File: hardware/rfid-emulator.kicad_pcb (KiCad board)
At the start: 4 copper layers, 150 x 72 mm, 102 parts, among them J1 AVR-JTAG-10, J2 Micro_USB, J3 OSTTC020162, Q1 2N3904, Q2 2N3906, Q3 2N3906, Q4 IRLML6344TRPBF, Q5 IRLML6344TRPBF, SW1 EN11-HSM1BF20, U1 NHD-C0216CiZ-FSW-FBW-3V3, U2 LT8613, U3 ATmega64A-AU, U4 MCP73832-2-OT, U5 LF33_TO252, U6 FT230XS, U7 LM324DT, Y1 ECS-160-20-5PX-TR

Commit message: Added silkscreen beaver
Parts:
- added G***: LOGO, logo:beaver2, F.Cu at (194.2, 98.9)
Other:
- board text removed: "RFID READER/EMULATOR"

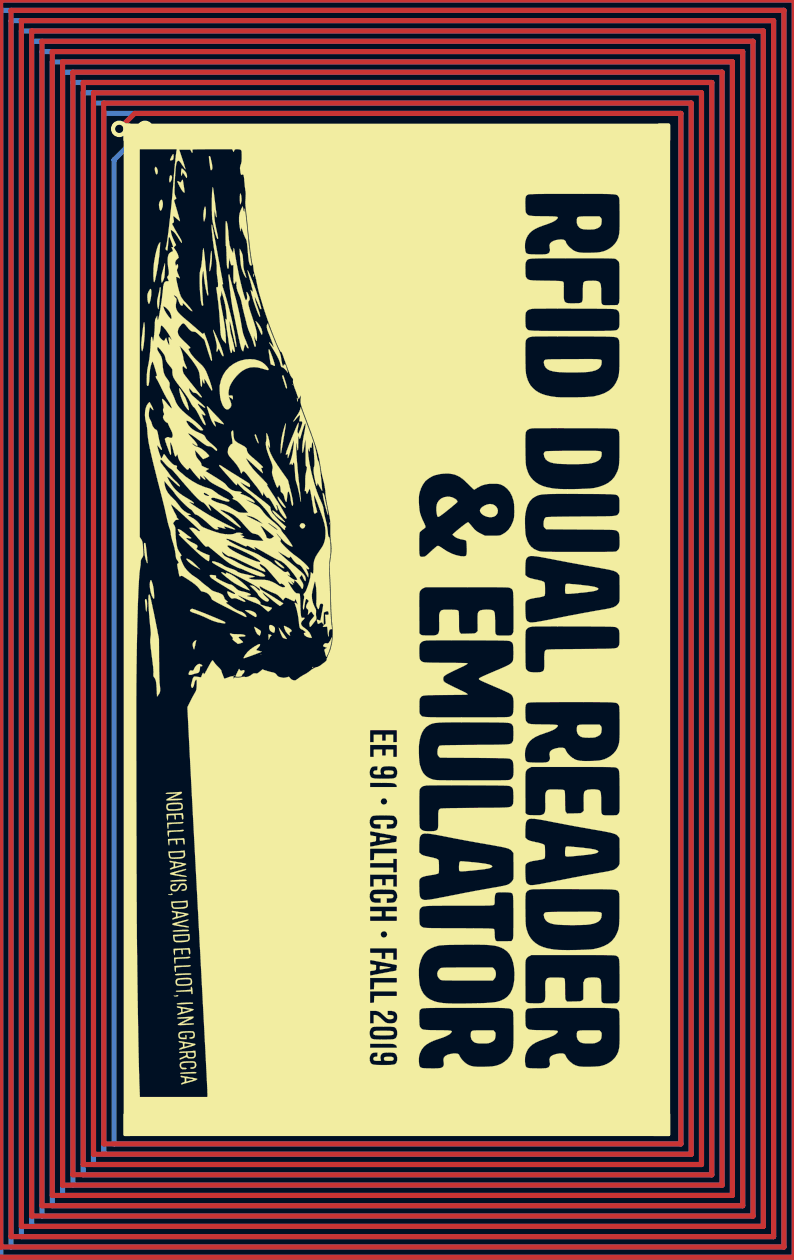
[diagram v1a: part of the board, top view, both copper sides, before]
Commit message: Fixed name typo
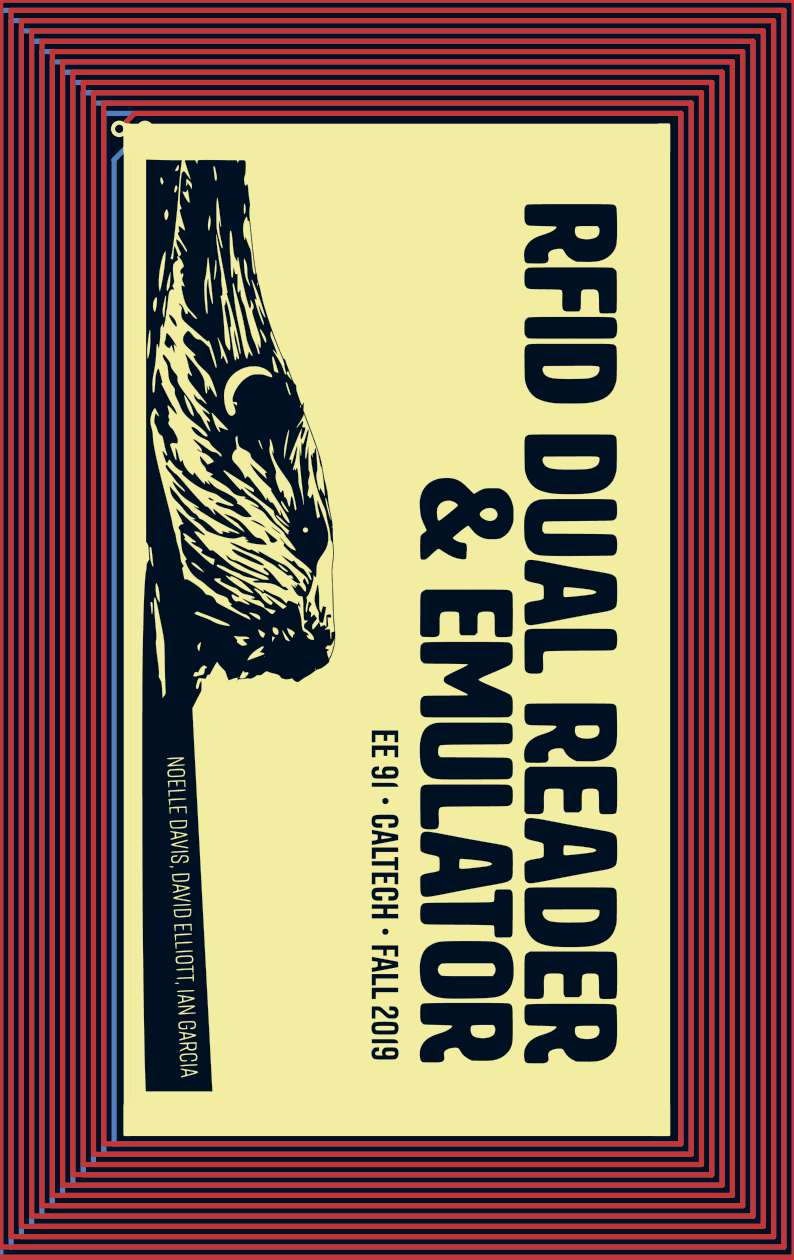
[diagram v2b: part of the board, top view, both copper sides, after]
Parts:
- moved G*** 0.14 mm to (194.3, 99.1)

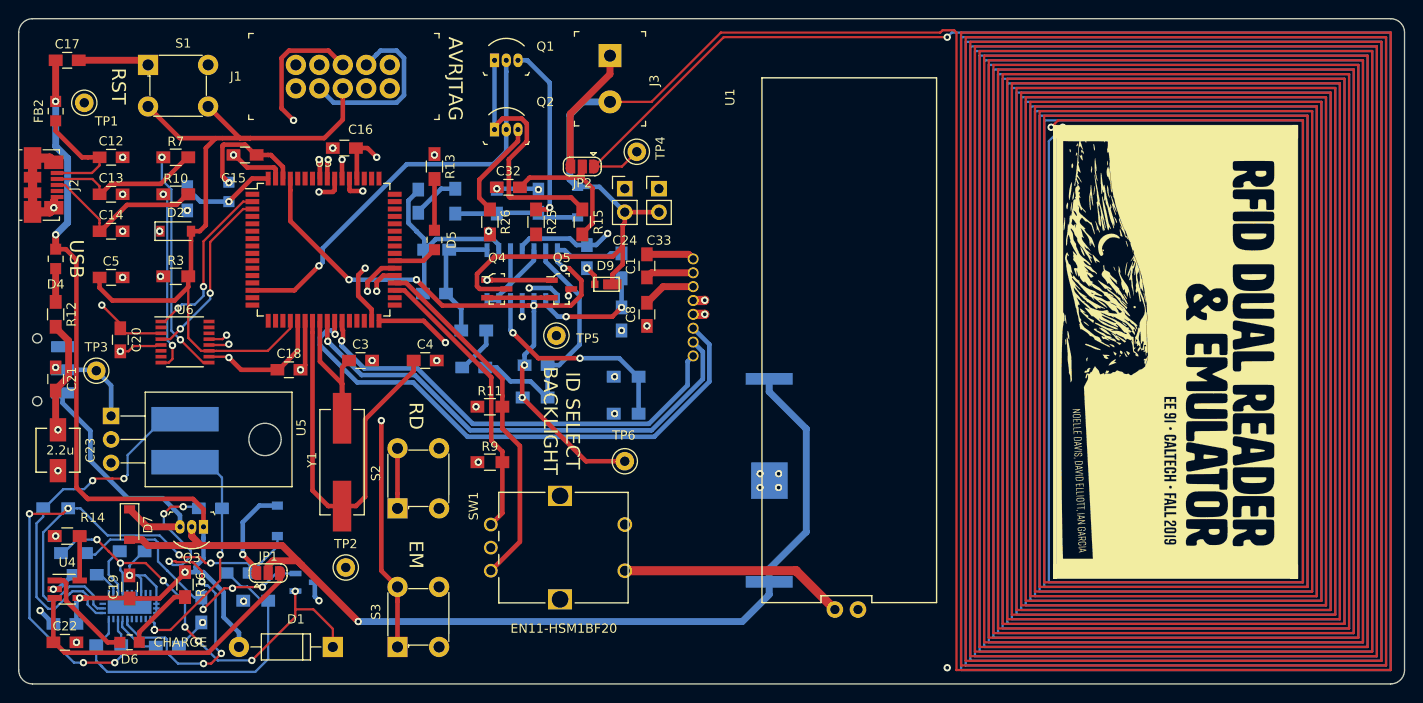
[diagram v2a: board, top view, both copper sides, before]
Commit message: Remove unnecessary components and apply fixes from V0.1
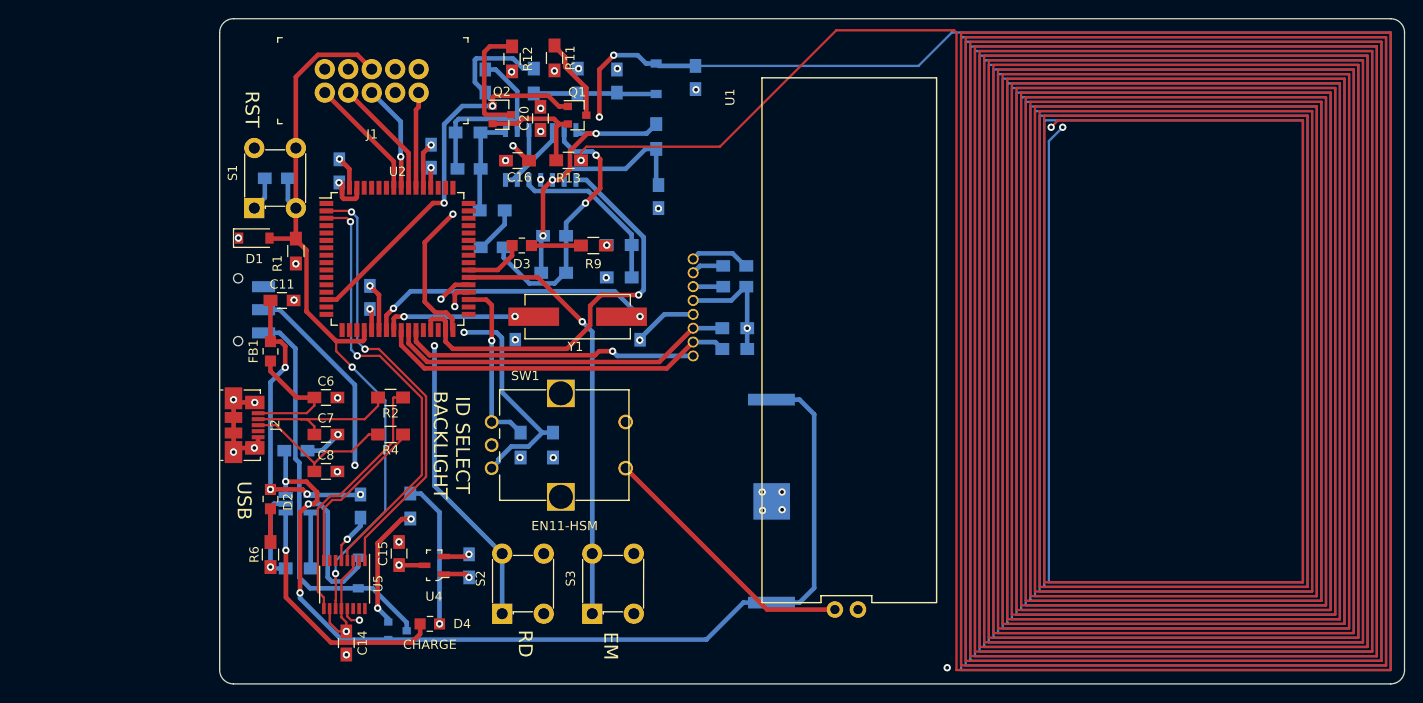
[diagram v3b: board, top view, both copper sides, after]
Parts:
- removed the C10 at (89.8, 116.0)
- removed the C12 at (79.0, 78.0)
- removed the C13 at (79.0, 82.0)
- removed the C17 at (74.2, 67.5)
- removed the C2 at (74.0, 128.5)
- removed the C20 at (80.0, 97.8)
- removed the C21 at (73.0, 102.0)
- removed the C23 at (73.2, 109.7)
- removed the C24 at (134.6, 81.4)
- removed C33: 0.0n, Socket_Strips:Socket_Strip_Straight_1x02_Pitch2.54mm
- removed the C9 at (87.2, 82.5)
- removed the D1 at (103.0, 131.0)
- removed the D4 at (73.0, 89.0)
- removed the D5 at (114.0, 87.0)
- removed D9: D_TVS, rfid-footprints:DO-219AD
- removed FB2: BLM21PG331SN1D, digikey-footprints:0805
- removed G***: LOGO, logo:beaver2
- removed J3: OSTTC020162, digikey-footprints:Term_Block_1x2_P5mm
- removed JP1: CHARGE_SELECT, Jumper:SolderJumper-3_P1.3mm_Open_RoundedPad1.0x1.5mm
- removed JP2: ANT_SELECT, Jumper:SolderJumper-3_P1.3mm_Open_RoundedPad1.0x1.5mm
- removed L1: 3.9u, rfid-footprints:CDRH6D28
- removed Q4, Q5: IRLML6344TRPBF, digikey-footprints:SOT-23-3
- removed the R1 at (74.9, 120.8)
- removed the R10 at (86.0, 82.0)
- removed the R11 at (120.0, 105.0)
- removed R26: 100, Resistors_SMD:R_0805_HandSoldering
- removed TP1: 5001, digikey-footprints:Test_Point_D1.02mm
- removed TP2, TP3: 5000, digikey-footprints:Test_Point_D1.02mm
- removed TP4, TP5, TP6: 5002, digikey-footprints:Test_Point_D1.02mm
- removed the U3 at (102.0, 88.0)
- removed the U6 at (87.0, 98.0)
- removed VR1: TL431AIDBZR, digikey-footprints:SOT-23-3
- added C15: 0.1u, Capacitors_SMD:C_0805_HandSoldering, F.Cu at (110.2, 120.9)
- added C18: 1u, Capacitors_SMD:C_0805_HandSoldering, B.Cu at (117.7, 122.2)
- added C19: 2.7n, Capacitors_SMD:C_0805_HandSoldering, B.Cu at (142.2, 69.4)
- added C8: 47p, Capacitors_SMD:C_0805_HandSoldering, F.Cu at (102.2, 112.0)
- added D2: LTST-C171KRKT, digikey-footprints:0805, F.Cu at (96.2, 115.0)
- added U4: MCP1700T-3302E_TT, digikey-footprints:SOT-23-3, F.Cu at (114.0, 122.2)
- C1: moved to B.Cu
- C10: renamed from C16; moved to B.Cu
- C11: value 10p -> 0.1u; moved to F.Cu
- C12: renamed from C18; moved to B.Cu
- C13: renamed from C19; moved to B.Cu
- C14: value 47p -> 0.1u
- C17: renamed from C22; moved to B.Cu
- C2: renamed from C3; moved to B.Cu
- C20: renamed from C25; moved to F.Cu
- C3: renamed from C4; moved to B.Cu
- C4: renamed from C5; moved to B.Cu
- C5: renamed from C8; moved to B.Cu
- C6: value 1u -> 10n; moved to F.Cu
- C7: value 1n -> 47p; moved to F.Cu
- C9: renamed from C15; moved to B.Cu
- D3: value 1N4148W -> LTST-C171KRKT; footprint Diodes_SMD:D_SOD-123 -> digikey-footprints:0805; moved to F.Cu
- D5: renamed from D7; moved to B.Cu
- FB1: moved to F.Cu
- J1: footprint digikey-footprints:PinHeader_2x5_P2.54mm_Drill1.2mm -> rfid-footprints:jtag-header
- Q1: value 2N3904 -> BC847; footprint digikey-footprints:TO-92-3 -> TO_SOT_Packages_SMD:SOT-23
- Q2: value 2N3906 -> BC857; footprint digikey-footprints:TO-92-3 -> TO_SOT_Packages_SMD:SOT-23
- Q3: value 2N3906 -> BC857; footprint digikey-footprints:TO-92-3 -> TO_SOT_Packages_SMD:SOT-23; moved to B.Cu
- R10: renamed from R14; moved to B.Cu
- R12: value 220k -> 100
- R14: renamed from R16; moved to B.Cu
- R2: value 10k -> 27; moved to F.Cu
- R3: renamed from R9; moved to B.Cu
- R4: value 60.4k -> 27; moved to F.Cu
- R5: value 1M -> 10k
- R6: value 243k -> 220k; moved to F.Cu
- R7: value 27 -> 4.7k; moved to B.Cu
- R8: value 8m -> 4.7k
- SW1: value EN11-HSM1BF20 -> EN11-HSM
- U2: value LT8613 -> ATmega64A-AU; footprint Housings_DFN_QFN:QFN-28-1EP_3x6mm_Pitch0.5mm -> Housings_QFP:TQFP-64_14x14mm_Pitch0.8mm; moved to F.Cu
- U3: renamed from U4; moved to B.Cu
- U5: value LF33_TO252 -> FT230XS; footprint TO_SOT_Packages_THT:TO-220-3_Horizontal -> Package_SO:SSOP-16_3.9x4.9mm_P0.635mm
- moved R8 76.0 mm to (146.5, 96.5)
- moved R7 64.0 mm to (146.5, 98.8), turned to 180 degrees
- moved R12 56.6 mm to (122.4, 67.3)
- moved R5 52.7 mm to (126.8, 109.2), turned to 90 degrees
- moved C14 51.3 mm to (104.5, 130.6), turned to 270 degrees
- moved U2 47.5 mm to (110.0, 89.0), turned to 0 degrees
- moved D3 39.8 mm to (123.5, 87.5), turned to 180 degrees
- moved J2 33.9 mm to (92.2, 107.0)
- moved D4 32.6 mm to (113.5, 128.5)
- moved C17 32.5 mm to (99.0, 109.8)
- moved C6 31.9 mm to (102.2, 104.0)
- moved U5 31.2 mm to (104.2, 124.2)
- moved R2 30.8 mm to (109.2, 104.0), turned to 180 degrees
- moved R4 30.7 mm to (109.2, 108.0), turned to 180 degrees
- moved C7 30.2 mm to (102.2, 108.0)
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- renumbered C32 to C16, C26 to C21, C27 to C22, C28 to C23, C29 to C24, C30 to C25, C31 to C26, D2 to D1, D6 to D4, D8 to D6, R3 to R1, R25 to R11, R15 to R13, R17 to R15, R18 to R16, R19 to R17, R20 to R18, R21 to R19, R22 to R20, R23 to R21, R24 to R22, R13 to R9, U7 to U6
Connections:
- net /DATA_IN_AN renamed Net-(C26-Pad1)
- BT1 pad 1: Net-(BT1-Pad1) -> /CHARGE_MCP
- C11 pad 1: Net-(C11-Pad1) -> /USB_VBUS
- C11 pad 2: Net-(C11-Pad2) -> GND
- C14 pad 1: Net-(C14-Pad1) -> +3V3
- C16 pad 2: Net-(C32-Pad2) -> /ANTENNA
- C2 pad 1: Net-(C3-Pad1) -> Net-(C2-Pad1)
- C3 pad 1: Net-(C4-Pad1) -> Net-(C3-Pad1)
- C7 pad 1: GND -> Net-(C7-Pad1)
- C7 pad 2: Net-(C7-Pad2) -> GND
- D3 pad 1: /CHARGE_LT -> Net-(D3-Pad1)
- D3 pad 2: Net-(C11-Pad1) -> /STAT
- D5 pad 2: Net-(BT1-Pad1) -> /CHARGE_MCP
- FB1 pad 1: +3V3 -> Net-(C6-Pad1)
- FB1 pad 2: Net-(C9-Pad1) -> /USB_VBUS
- J1 pad 8: Net-(J1-Pad8) -> (no net)
- J2 pad 1: Net-(C12-Pad1) -> Net-(C6-Pad1)
- J2 pad 2: Net-(C13-Pad1) -> Net-(C7-Pad1)
- J2 pad 3: Net-(C14-Pad1) -> Net-(C8-Pad1)
- J2 pad 4: Net-(J2-Pad4) -> (no net)
- Q1 pad 1: Net-(Q1-Pad1) -> /OC0
- Q1 pad 2: /OC0 -> Net-(Q1-Pad2)
- Q2 pad 1: Net-(Q1-Pad1) -> /OC0
- Q2 pad 2: /OC0 -> Net-(Q1-Pad2)
- Q3 pad 1: /USB_VBUS -> /CHARGE_MCP
- Q3 pad 2: Net-(BT1-Pad1) -> /USB_VBUS
- R11 pad 2: +5V -> +3V3
- R12 pad 1: Net-(D4-Pad2) (its old number) -> Net-(Q2-Pad3)
- R13 pad 1: Net-(C32-Pad2) -> /ANTENNA
- R13 pad 2: Net-(Q1-Pad1) -> Net-(Q1-Pad2)
- R2 pad 1: Net-(R1-Pad2) -> /USB_D-
- R2 pad 2: GND -> Net-(C7-Pad1)
- R3 pad 2: Net-(R9-Pad2) -> Net-(R3-Pad2)
- R4 pad 1: Net-(R4-Pad1) -> /USB_D+
- R4 pad 2: GND -> Net-(C8-Pad1)
- R5 pad 1: Net-(C11-Pad2) -> +3V3
- R5 pad 2: Net-(C11-Pad1) -> Net-(R5-Pad2)
- R6 pad 1: GND -> Net-(D2-Pad2)
- R6 pad 2: Net-(C11-Pad2) -> GND
- R7 pad 1: /USB_D- -> +3V3
- R7 pad 2: Net-(C13-Pad1) -> /I2C_SCL
- R8 pad 1: Net-(C11-Pad1) -> +3V3
- R8 pad 2: Net-(L1-Pad1) -> /I2C_SDA
- R9 pad 2: Net-(D5-Pad1) (its old number) -> Net-(D3-Pad1)
- S4 pad 3: Net-(S4-Pad3) -> (no net)
- SW1 pad A: Net-(R9-Pad2) -> Net-(R3-Pad2)
- SW1 pad B: Net-(R11-Pad2) -> Net-(R5-Pad2)
- U2 pad 1: Net-(U2-Pad1) -> (no net)
- U2 pad 11: GND -> (no net)
- U2 pad 14: (no net) -> /OC0
- U2 pad 15: Net-(C10-Pad2) -> (no net)
- U2 pad 2: Net-(C7-Pad2) -> /UART0_RX
- U2 pad 20: Net-(C10-Pad1) -> /~RESET~
- U2 pad 21: Net-(C6-Pad1) -> +3V3
- U2 pad 22: Net-(C11-Pad1) -> GND
- U2 pad 23: Net-(U2-Pad23) -> Net-(C3-Pad1)
- U2 pad 24: Net-(C11-Pad2) -> Net-(C2-Pad1)
- U2 pad 25: Net-(L1-Pad1) -> /I2C_SCL
- U2 pad 26: Net-(C11-Pad1) -> /I2C_SDA
- U2 pad 27: Net-(U2-Pad27) -> /~I2C_RST~
- U2 pad 28: Net-(U2-Pad28) -> (no net)
- U2 pad 29: (no net) -> /DATA_IN
- U2 pad 3: Net-(R4-Pad1) -> /UART0_TX
- U2 pad 4: Net-(D1-Pad1) -> (no net)
- U2 pad 5: Net-(D1-Pad1) -> (no net)
- U2 pad 8: GND -> (no net)
- U5 pad 1: /VSUPPLY -> /UART0_RX
- U5 pad 2: GND -> (no net)
- U6 pad 8: /DATA_IN_DIG -> /DATA_IN
- Y1 pad 1: Net-(C3-Pad1) -> Net-(C2-Pad1)
- Y1 pad 2: Net-(C4-Pad1) -> Net-(C3-Pad1)
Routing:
- net Net-(BT1-Pad1): track 114.6 -> 0.00 mm, vias 1 -> 0
- net /CHARGE_MCP: track 34.7 -> 119.9 mm, vias 0 -> 3
- net Net-(C11-Pad1): track 80.8 -> 0.00 mm, vias 6 -> 0
- net Net-(C26-Pad1): track 79.0 -> 27.8 mm, vias 6 -> 3
- net Net-(D1-Pad1): track 48.5 -> 0.00 mm, vias 7 -> 0
- net /DATA_IN: track 0.00 -> 46.3 mm, vias 0 -> 1
- net /USB_VBUS: track 98.3 -> 52.7 mm, vias 4 -> 6
- net Net-(C4-Pad1): track 42.1 -> 0.00 mm
- net Net-(C10-Pad1): track 41.0 -> 0.00 mm, vias 6 -> 0
- net Net-(L1-Pad1): track 40.6 -> 0.00 mm, vias 2 -> 0
- net Net-(R11-Pad2): track 38.8 -> 0.00 mm
- net +3V3: track 75.2 -> 37.2 mm, vias 15 -> 13
- net Net-(C11-Pad2): track 37.2 -> 0.00 mm
- net /DATA_OUT: track 35.6 -> 0.00 mm, vias 2 -> 0
- net Net-(R9-Pad2): track 31.3 -> 0.00 mm
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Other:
- board size 150 x 72 mm -> 128.2 x 72 mm
- board text removed: "AVRJTAG"
